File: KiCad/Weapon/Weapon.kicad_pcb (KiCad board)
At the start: 2 copper layers, 97.3 x 68.5 mm, 33 parts, among them IC1 ATMEGA328-P, J1 MICRO_USB, P1 2P_CGRID_M, P2 USB-TTL, P3 2P_CGRID_M, Q1 NPN, Q2 NPN, U1 MCP73831, U2 RFID-RC522, U3 LM1084IT-3.3/NOPB, X1 16MHz

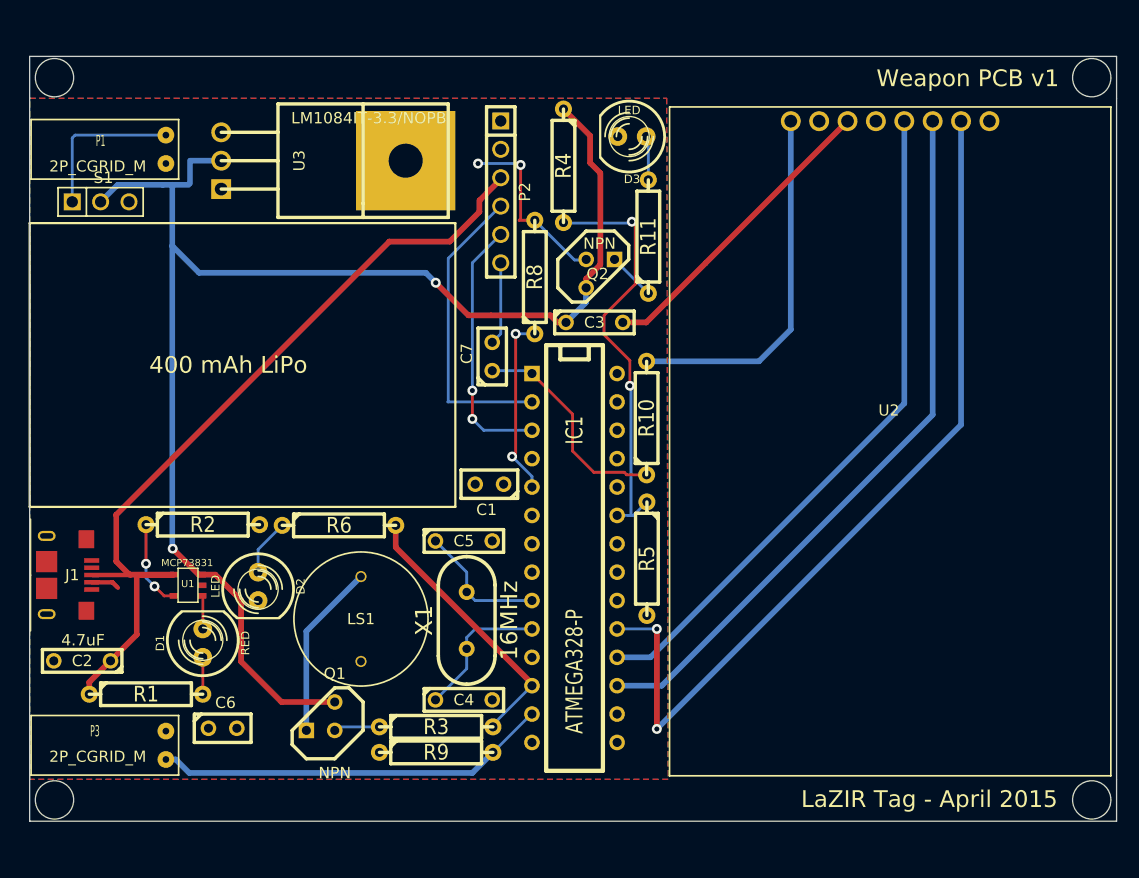
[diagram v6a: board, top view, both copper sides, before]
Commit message: Quick Update #6 4/16
Hopefully the last changes to the ir receiver pcb and weapon pcb
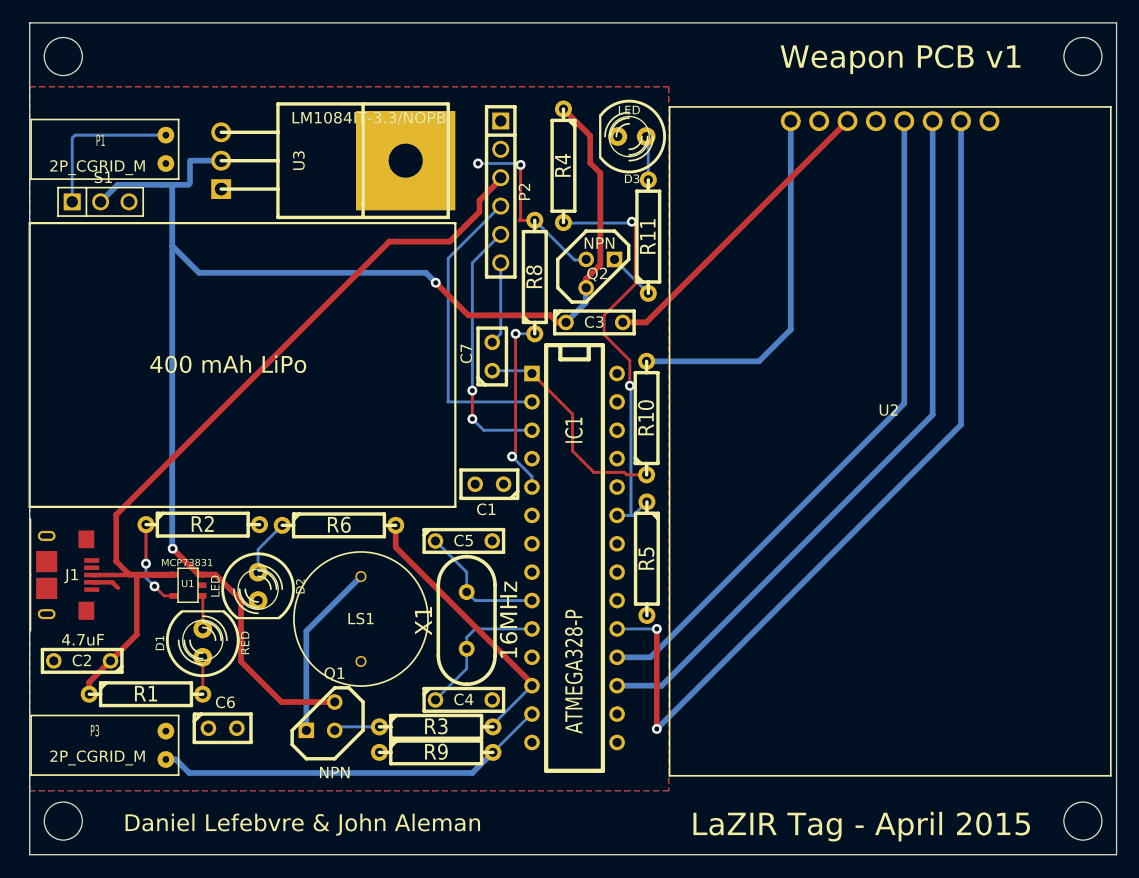
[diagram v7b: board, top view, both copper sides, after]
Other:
- board size 97.3 x 68.5 mm -> 97.3 x 74.4 mm
- board text added: "Daniel Lefebvre & John Aleman"
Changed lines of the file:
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@@
   (general
     (links 65)
-    (no_connects 1)
+    (no_connects 0)
     (area 32.002999 20.079499 129.590001 88.632501)
     (thickness 1.6)
-    (drawings 21)
+    (drawings 26)
     (tracks 175)
     (zones 0)
@@
     )
   )
-  (gr_circle (center 127.3175 22.0345) (end 129.032 22.0345) (layer Edge.Cuts) (width 0.1))
-  (gr_circle (center 34.4805 22.0345) (end 36.195 22.0345) (layer Edge.Cuts) (width 0.1))
-  (gr_circle (center 34.4805 86.6775) (end 36.195 86.6775) (layer Edge.Cuts) (width 0.1))
-  (gr_circle (center 127.3175 86.6775) (end 129.032 86.6775) (layer Edge.Cuts) (width 0.1))
+  (gr_text "Daniel Lefebvre & John Aleman" (at 56.6928 88.773) (layer F.SilkS)
+    (effects (font (size 1.5 1.5) (thickness 0.3)))
+  )
+  (gr_circle (center 126.5301 88.5698) (end 124.8283 88.5698) (layer Edge.Cuts) (width 0.1))
+  (gr_circle (center 35.2679 88.5698) (end 36.9697 88.5698) (layer Edge.Cuts) (width 0.1))
+  (gr_circle (center 126.5301 20.1422) (end 124.8283 20.1422) (layer Edge.Cuts) (width 0.1))
+  (gr_circle (center 35.2679 20.1422) (end 36.9697 20.1422) (layer Edge.Cuts) (width 0.1))
+  (gr_line (start 129.54 91.5797) (end 129.54 88.5825) (angle 90) (layer Edge.Cuts) (width 0.1))
+  (gr_line (start 32.258 91.5797) (end 129.54 91.5797) (angle 90) (layer Edge.Cuts) (width 0.1))
+  (gr_line (start 32.258 88.5825) (end 32.258 91.5797) (angle 90) (layer Edge.Cuts) (width 0.1))
+  (gr_line (start 129.54 17.1323) (end 129.54 20.1295) (angle 90) (layer Edge.Cuts) (width 0.1))
+  (gr_line (start 32.258 17.1323) (end 129.54 17.1323) (angle 90) (layer Edge.Cuts) (width 0.1))
+  (gr_line (start 32.258 20.1295) (end 32.258 17.1323) (angle 90) (layer Edge.Cuts) (width 0.1))
   (gr_line (start 129.54 20.1295) (end 129.54 23.876) (angle 90) (layer Edge.Cuts) (width 0.1))
-  (gr_line (start 32.258 20.1295) (end 129.54 20.1295) (angle 90) (layer Edge.Cuts) (width 0.1))
   (gr_line (start 32.258 23.876) (end 32.258 20.1295) (angle 90) (layer Edge.Cuts) (width 0.1))
   (gr_line (start 129.54 88.5825) (end 129.54 84.836) (angle 90) (layer Edge.Cuts) (width 0.1))
-  (gr_line (start 32.258 88.5825) (end 129.54 88.5825) (angle 90) (layer Edge.Cuts) (width 0.1))
   (gr_line (start 32.258 84.836) (end 32.258 88.5825) (angle 90) (layer Edge.Cuts) (width 0.1))
   (gr_line (start 129.54 23.876) (end 129.54 84.836) (angle 90) (layer Edge.Cuts) (width 0.1))
-  (gr_text "LaZIR Tag - April 2015" (at 97.0915 86.614) (layer B.SilkS)
-    (effects (font (size 1.5 1.5) (thickness 0.3)) (justify right mirror))
-  )
-  (gr_text "Weapon PCB v1" (at 106.68 22.098) (layer B.SilkS)
-    (effects (font (size 1.5 1.5) (thickness 0.3)) (justify right mirror))
+  (gr_text "LaZIR Tag - April 2015" (at 85.7504 88.9) (layer B.SilkS)
+    (effects (font (size 2 2) (thickness 0.3)) (justify right mirror))
+  )
+  (gr_text "Weapon PCB v1" (at 97.2693 20.193) (layer B.SilkS)
+    (effects (font (size 2 2) (thickness 0.3)) (justify right mirror))
   )
   (gr_line (start 32.258 84.836) (end 32.258 23.876) (angle 90) (layer Edge.Cuts) (width 0.1))
-  (gr_text "Weapon PCB v1" (at 124.3965 22.098) (layer F.SilkS)
-    (effects (font (size 1.5 1.5) (thickness 0.3)) (justify right))
-  )
-  (gr_text "LaZIR Tag - April 2015" (at 124.2695 86.614) (layer F.SilkS)
-    (effects (font (size 1.5 1.5) (thickness 0.3)) (justify right))
+  (gr_text "Weapon PCB v1" (at 121.1834 20.2184) (layer F.SilkS)
+    (effects (font (size 2 2) (thickness 0.3)) (justify right))
+  )
+  (gr_text "LaZIR Tag - April 2015" (at 122.0343 88.9) (layer F.SilkS)
+    (effects (font (size 2 2) (thickness 0.3)) (justify right))
   )
   (gr_text "400 mAh LiPo" (at 50.038 47.752) (layer F.SilkS)
@@
     )
   )
+  (zone (net 1) (net_name +3.3V) (layer B.Cu) (hatch edge 0.508)
+    (connect_pads (clearance 0.508))
+    (min_thickness 0.254)
+    (fill (arc_segments 16) (thermal_gap 0.508) (thermal_bridge_width 0.508))
+    (polygon
+      (pts
+        (xy 89.4588 85.8647) (xy 32.258 85.8647) (xy 32.258 22.8473) (xy 89.4588 22.8473)
+      )
+    )
+  )
   (zone (net 2) (net_name GND) (layer F.Cu) (hatch edge 0.508)
     (connect_pads (clearance 0.508))
@@
     (polygon
       (pts
-        (xy 89.408 84.836) (xy 32.258 84.836) (xy 32.258 23.876) (xy 89.281 23.876)
+        (xy 89.4588 85.8647) (xy 32.258 85.8647) (xy 32.258 22.8473) (xy 89.4588 22.8473)
       )
     )
-  )
-  (zone (net 1) (net_name +3.3V) (layer B.Cu) (hatch edge 0.508)
-    (connect_pads (clearance 0.508))
-    (min_thickness 0.254)
-    (fill (arc_segments 16) (thermal_gap 0.508) (thermal_bridge_width 0.508))
-    (polygon
-      (pts
-        (xy 89.408 84.836) (xy 32.258 84.836) (xy 32.258 23.876) (xy 89.281 23.876)
-      )
-    )
-  )
-  (zone (net 0) (net_name "") (layer F.Cu) (hatch edge 0.508)
-    (connect_pads (clearance 0.508))
-    (min_thickness 0.254)
-    (keepout (tracks allowed) (vias allowed) (copperpour not_allowed))
-    (fill (arc_segments 16) (thermal_gap 0.508) (thermal_bridge_width 0.508))
-    (polygon
-      (pts
-        (xy 70.358 60.452) (xy 32.258 60.452) (xy 32.258 35.052) (xy 70.358 35.052)
-      )
-    )

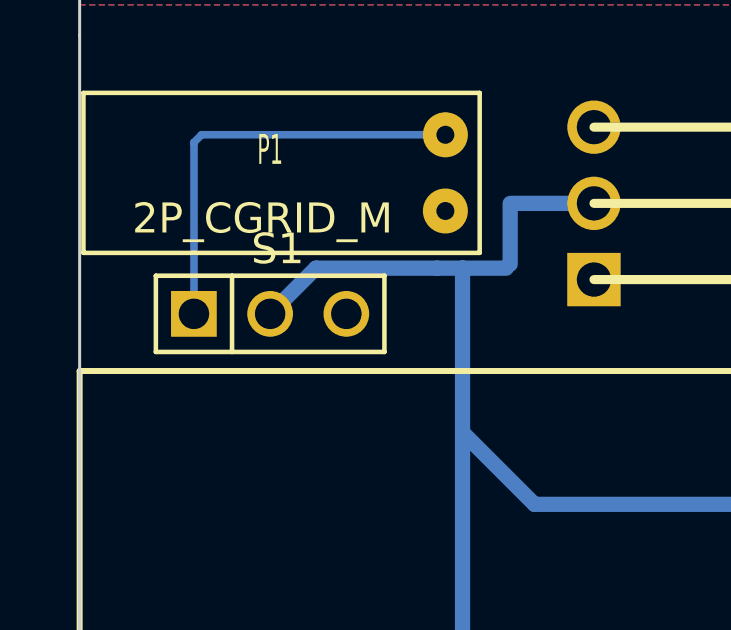
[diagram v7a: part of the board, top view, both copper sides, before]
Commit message: Update #1 4/17
First Draft of Player/Health PCB for review.
Added on/off indicators to weapon pcb for slideswitch
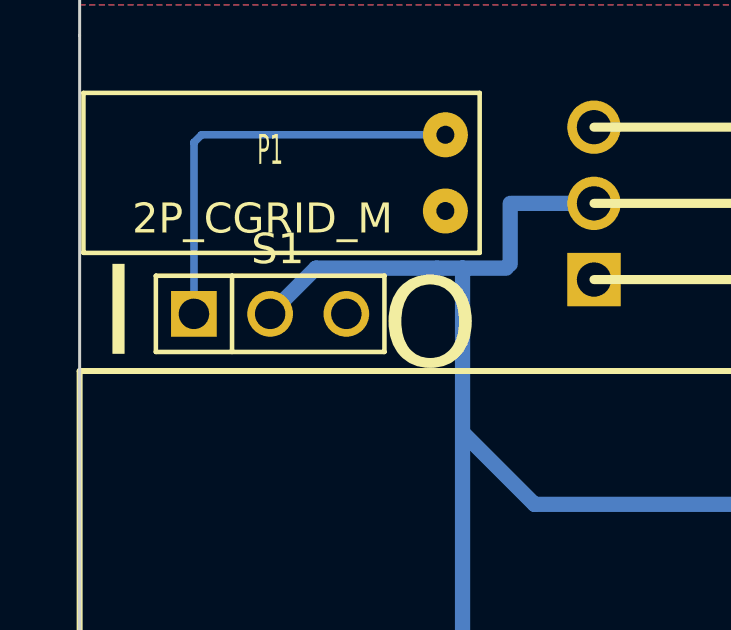
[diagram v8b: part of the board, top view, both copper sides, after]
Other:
- board text added: "I"
- board text added: "O"
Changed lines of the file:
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@@
     (links 65)
     (no_connects 0)
-    (area 32.002999 20.079499 129.590001 88.632501)
+    (area 32.002999 17.082299 129.590001 91.629701)
     (thickness 1.6)
-    (drawings 26)
+    (drawings 28)
     (tracks 175)
     (zones 0)
@@
     )
   )
+  (gr_text I (at 33.5534 32.8676 180) (layer F.SilkS)
+    (effects (font (size 3 3) (thickness 0.3)))
+  )
+  (gr_text O (at 43.942 33.5026) (layer F.SilkS)
+    (effects (font (size 3 3) (thickness 0.3)))
+  )
   (gr_text "Daniel Lefebvre & John Aleman" (at 56.6928 88.773) (layer F.SilkS)
